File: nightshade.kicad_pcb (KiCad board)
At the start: 4 copper layers, 187.3 x 75.4 mm, 99 parts, among them J1 Bus_ISA_16bit, J2 DE15_Plug_HighDensity_Mountin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, J3 Conn_02x13_Odd_Even, Q1 MMBT3904, U1 GD542x_ISA, U10 74HCT244, U11 SOJ_256Kx16, U12 SOJ_256Kx16, U2 SOJ_256Kx16, U3 SOJ_256Kx16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

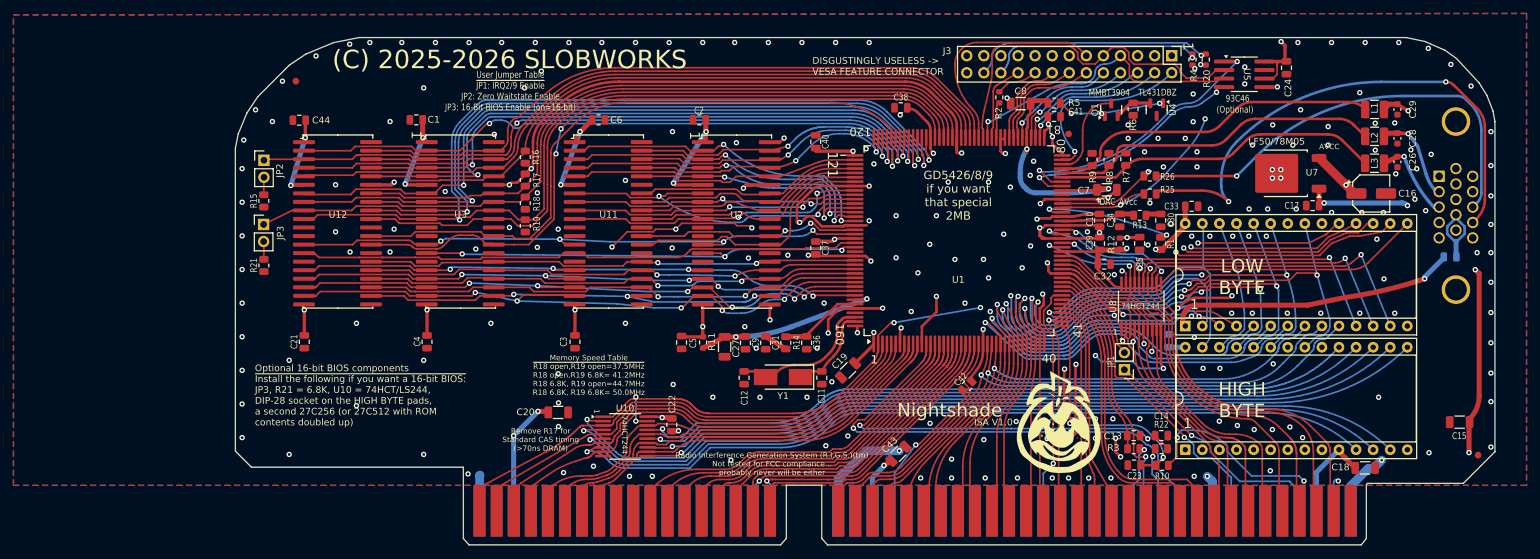
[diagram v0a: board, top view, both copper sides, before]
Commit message: Add files via upload
A big bunch of little bug fixes, and combined a capacitor and DIP-28 socket to fix an issue where a ceramic cap was placed too close to the edge connector (mechanical stress issue).
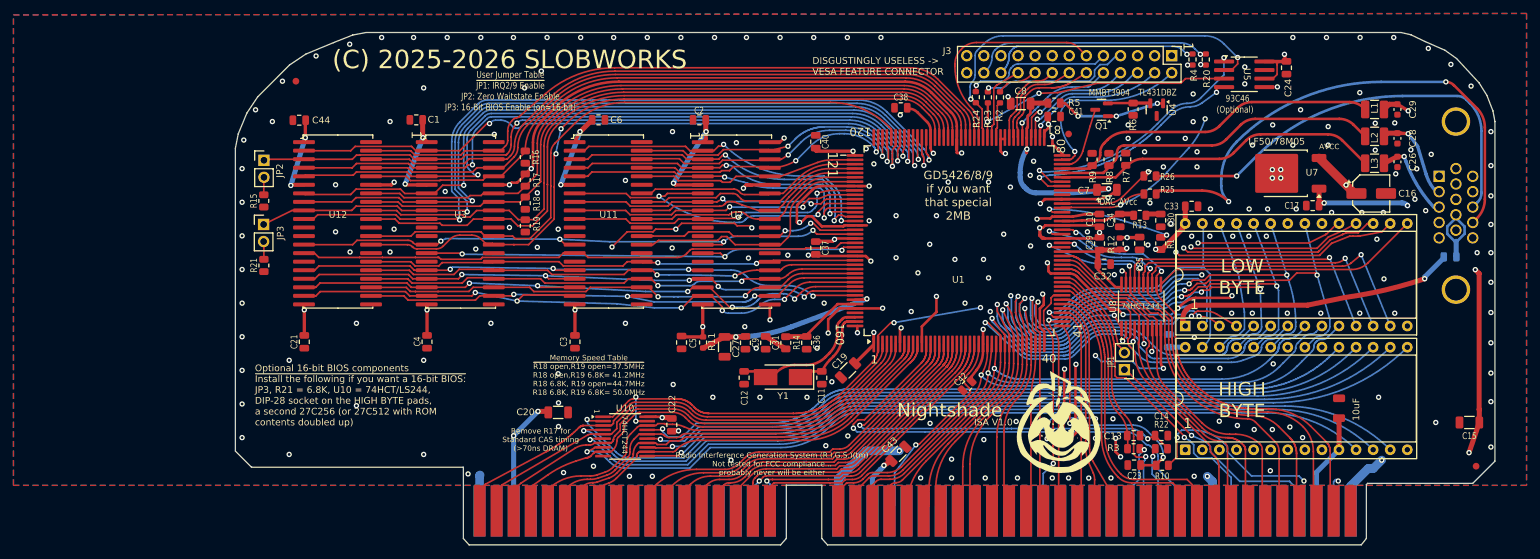
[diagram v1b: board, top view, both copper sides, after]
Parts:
- removed C18: 10u, Capacitor_SMD:C_1206_3216Metric
- added R23: 1K, Resistor_SMD:R_0603_1608Metric, F.Cu at (158.9, 91.4)
- added R24: 1K, Resistor_SMD:R_0603_1608Metric, F.Cu at (157.1, 91.4)
- U9: footprint Package_DIP:DIP-28_W15.24mm_Socket -> PDVGA:DIP-28_W15.24mm_Plus_Cap_Socket
- moved FID2 1.68 mm to (231.5, 146.2)
- moved C15 1.45 mm to (230.5, 139.8)
- moved Q1 1.44 mm to (175.8, 93.2), turned to 180 degrees
- moved R2 0.10 mm to (160.7, 91.4)
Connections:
- J3 pad 7: /EVIDEO -> Net-(J3-Pin_7)
- J3 pad 9: /ESYNC -> Net-(J3-Pin_9)
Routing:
- net Net-(J3-Pin_7): track 0.00 -> 22.6 mm, vias 0 -> 1
- net Net-(J3-Pin_9): track 0.00 -> 22.0 mm, vias 0 -> 1
- net /ESYNC: track 53.5 -> 58.1 mm, vias 0 -> 2
- net /IREF: track 13.7 -> 10.4 mm
- net /EVIDEO: track 43.5 -> 45.6 mm, vias 1 -> 2
- net /EECS: track 42.5 -> 40.9 mm
- net /+5V: track 339.0 -> 340.1 mm
- net /FHSYNC: track 32.4 -> 31.4 mm
- net Net-(Q1-B): track 16.7 -> 17.6 mm
- net Net-(Q1-E): track 5.68 -> 6.40 mm
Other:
- board size 187.3 x 75.4 mm -> 187.3 x 76.2 mm
- board text added: "10uF"

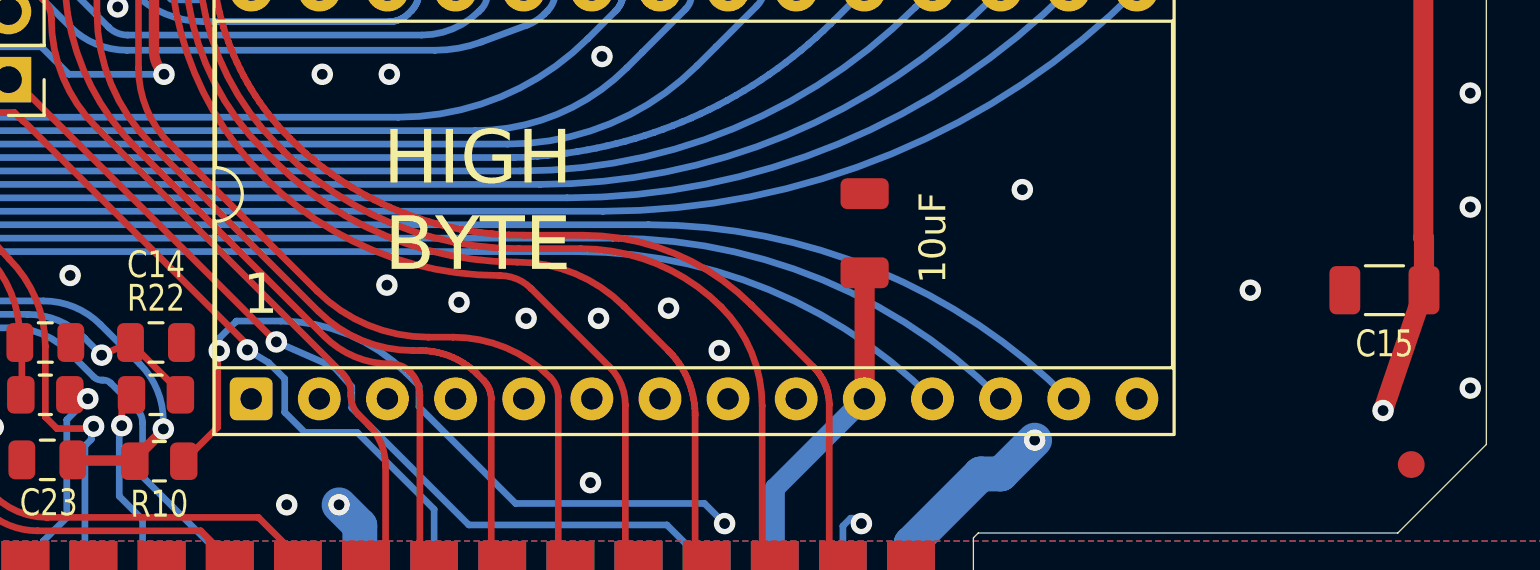
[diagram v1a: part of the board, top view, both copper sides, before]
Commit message: Add files via upload
Changed combined footprint back to discrete individual cap and socket. Moved capacitor out from underneath the socket footprint. There, automated assembly should be able to install everything now.
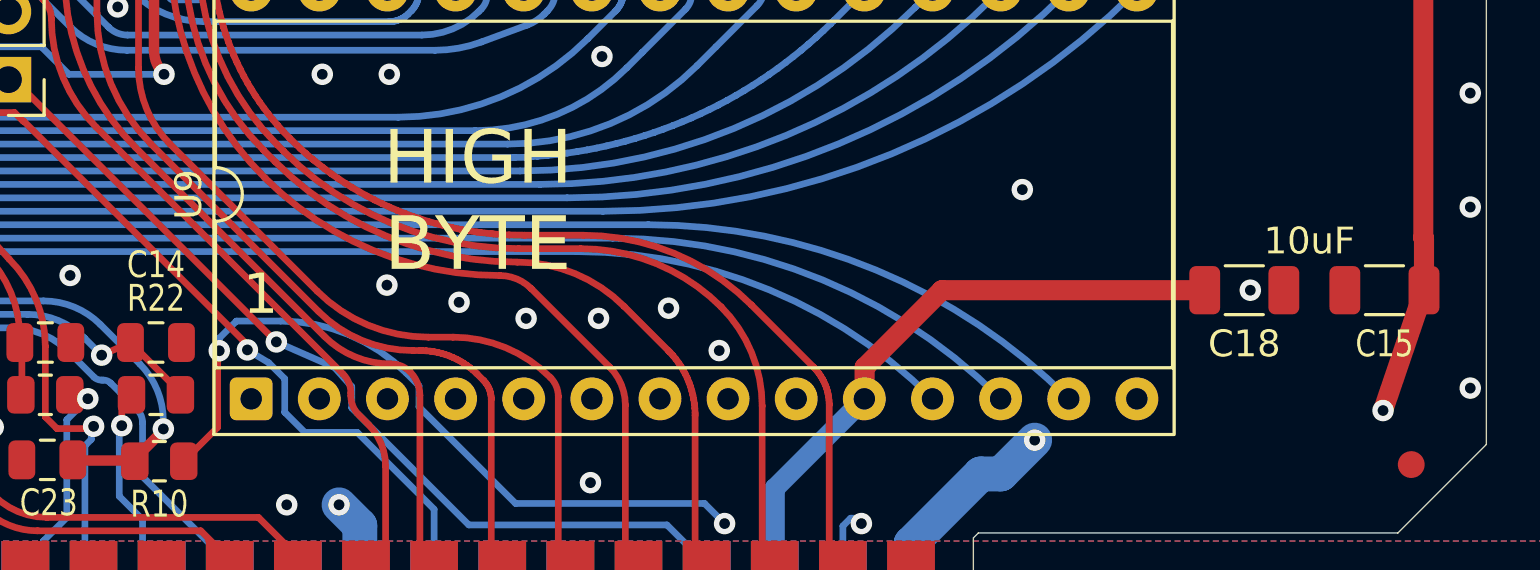
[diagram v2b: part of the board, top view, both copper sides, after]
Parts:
- added C18: 10u, Capacitor_SMD:C_1206_3216Metric, F.Cu at (225.3, 139.8)
- U9: footprint PDVGA:DIP-28_W15.24mm_Plus_Cap_Socket -> Package_DIP:DIP-28_W15.24mm_Socket
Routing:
- net /+5V: track 340.1 -> 350.5 mm

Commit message: Add files via upload
More minor fixes.
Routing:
- net GND: track 345.9 -> 344.8 mm
